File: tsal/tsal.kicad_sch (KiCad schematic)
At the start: 22 parts, among them J1 Conn_01x04, Q1 BUK7M9R5-40H, Q2 BUK7M9R5-40H

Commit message: feat(tsal): updated schematic and pcb
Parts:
- removed D1, D2, D6, D7: 150283RS73103, footprints:Wurth_WL-SMTW, symbol Device:LED
- removed D3, D4, D8, D9: 150283GS73103, footprints:Wurth_WL-SMTW, symbol Device:LED
- removed Q1, Q2: BUK7M9R5-40H, Package_TO_SOT_SMD:LFPAK33, symbol Transistor_FET:BUK7M9R9-60EX
- removed R1, R20, R22, R23, R3, R4: 27, Resistor_SMD:R_2512_6332Metric, symbol Device:R
- added H1, H2, H3: MountingHole, MountingHole:MountingHole_3.2mm_M3, symbol Mechanical:MountingHole
- added J2: Conn_01x03, Connector_Molex:Molex_Micro-Fit_3.0_43650-0315_1x03_P3.00mm_Vertical, symbol Connector_Generic:Conn_01x03
- added Q1, Q2: FDN359BN, Package_TO_SOT_SMD:SOT-23, symbol SUFST:FDN359BN
- J1: footprint Connector_Molex:Molex_Micro-Fit_3.0_43650-0400_1x04_P3.00mm_Horizontal -> Connector_Molex:Molex_Micro-Fit_3.0_43650-0415_1x04_P3.00mm_Vertical
- renumbered R21 to R1
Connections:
- net +12V: now also J2.1 (Pin_1)
- net GND: now also Q1.2 (S), Q2.2 (S)
- net at R2.1: now also J2.2 (Pin_2)
- net at R1.1: now also J2.3 (Pin_3)
- net at R1.2: now also Q1.3 (D)
- net at R2.2: now also Q2.3 (D)
- net GREEN_LED_ON renamed GREEN_LED ON
- net GREEN_LED ON: now also Q2.1 (G)
- net RED_LED_ON renamed RED_LED ON
- net RED_LED ON: now also Q1.1 (G)
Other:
- note removed: "LEDs rated for 180mA. ~3V drop each, so ~6V across resistor. R = 54 gives current of 110mA, and 0.33W in each resistor."
- company: (none) -> SUFST
- title: (none) -> TSAL Driver
- moved on the sheet: R1, R6

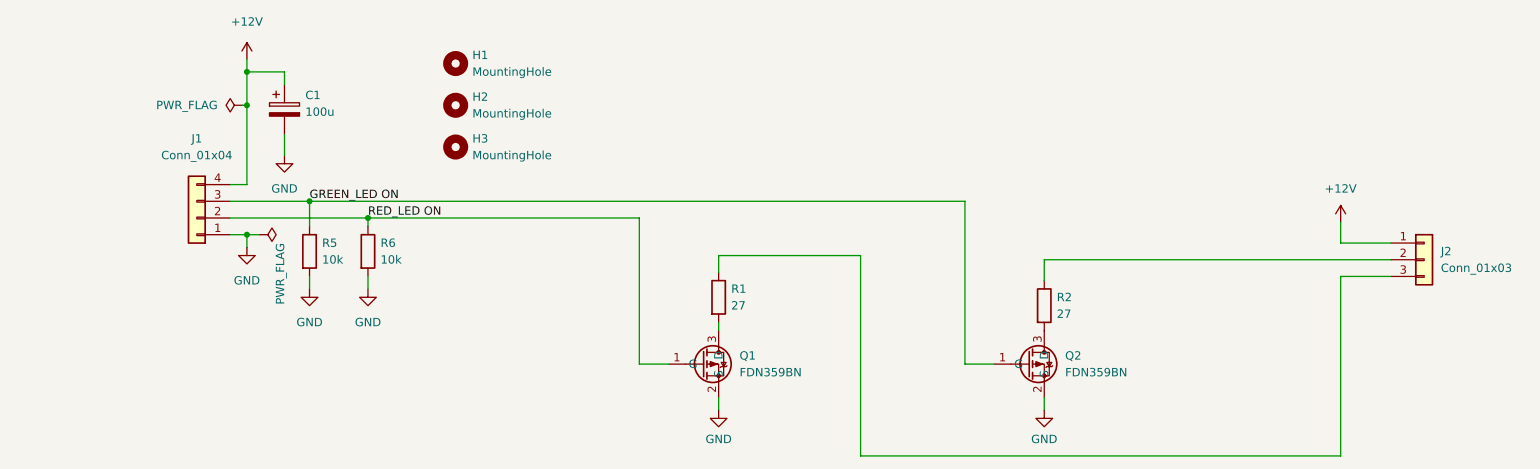
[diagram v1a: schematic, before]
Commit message: feat(tsal) added cad files for the connectors and comments to the schematics
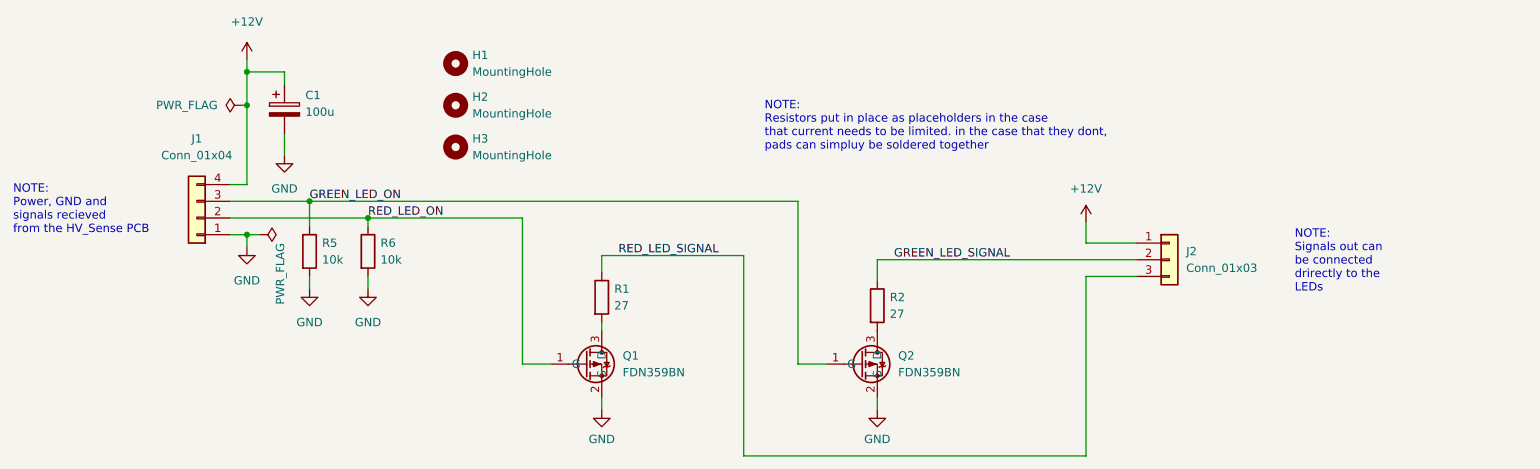
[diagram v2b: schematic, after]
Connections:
- net GREEN_LED_SIGNAL: now reaches J2.2 (Pin_2), R2.1
- net RED_LED_SIGNAL: now reaches J2.3 (Pin_3), R1.1
- net GREEN_LED ON renamed GREEN_LED_ON
- net RED_LED ON renamed RED_LED_ON
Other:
- note added: "NOTE: Power, GND and signals recieved from the HV_Sense PCB"
- note added: "NOTE: Resistors put in place as placeholders in the case that current needs to be limited. in the case that they dont, pads can simpluy be soldered together"
- note added: "NOTE: Signals out can be connected drirectly to the LEDs"
- moved on the sheet: J2, Q1, Q2, R1, R2

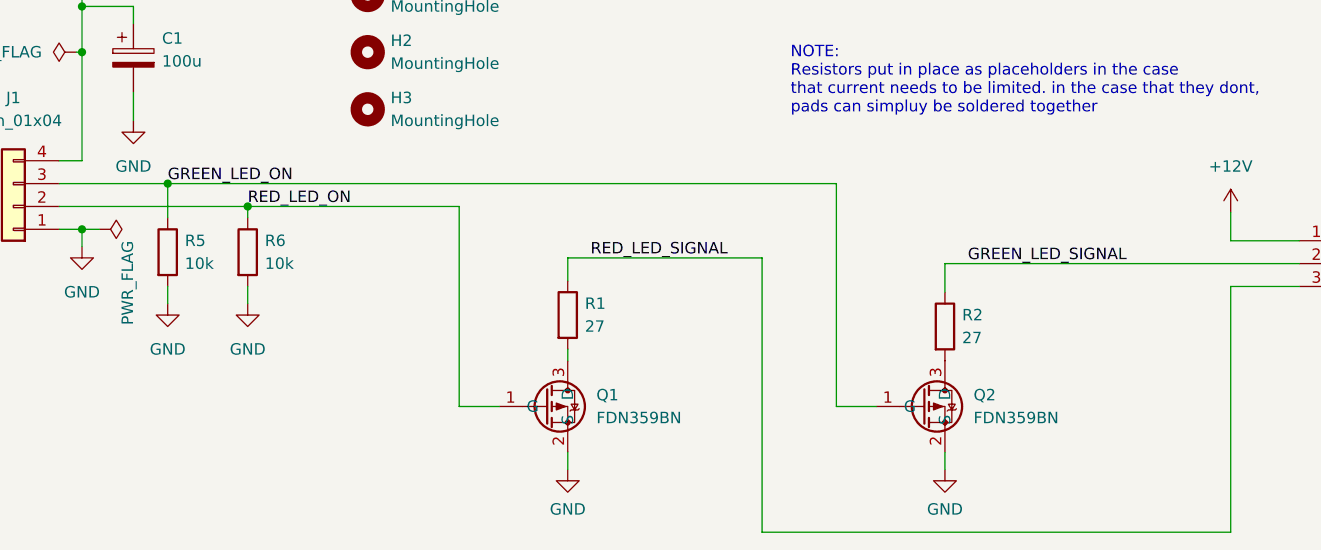
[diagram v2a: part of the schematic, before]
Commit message: feat(tsal) updated tsal driver pcb design: changes in routing, added 12V power plane, added via for Q2, made board smaller, hid mounting hole reference names, moved cad files into common, swapped green_led_on and red_led_on pins for simpler routing, added board name to board, moved symbols library from global to project specific
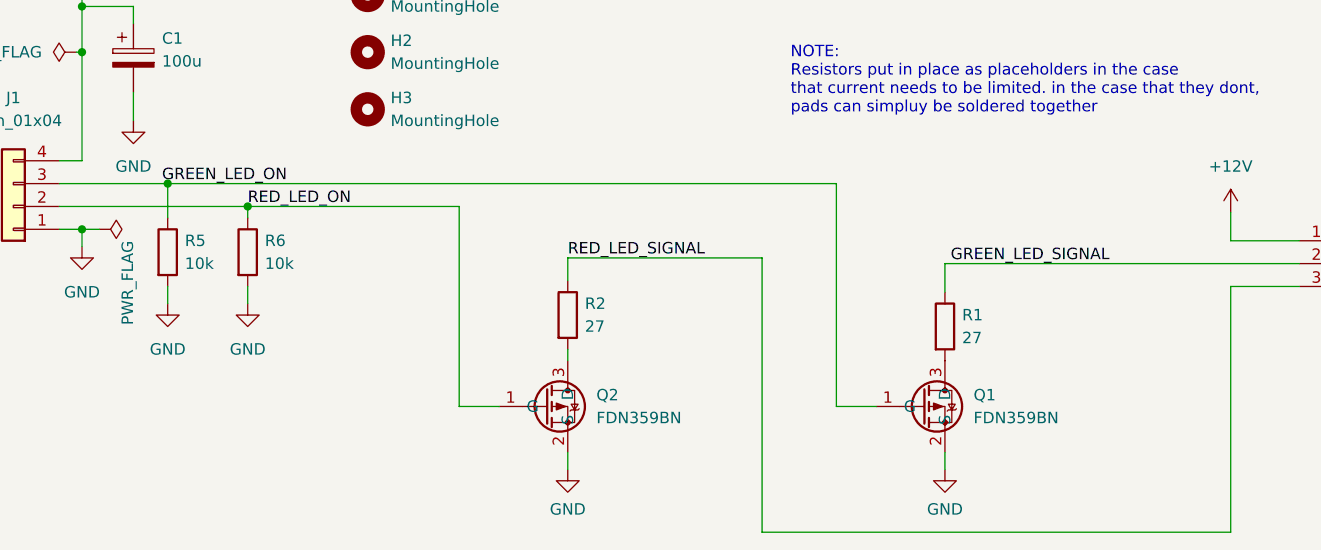
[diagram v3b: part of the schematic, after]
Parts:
- renumbered Q2 to Q1, Q1 to Q2, R2 to R1, R1 to R2
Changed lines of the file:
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@@
     (comment 1 "STAG 9")
     (comment 2 "Marek Frodyma")
+    (comment 3 "Tim Brewis")
   )
   (junction (at 74.295 100.965) (diameter 0) (color 0 0 0 0)
@@
     (effects (font (size 1.27 1.27)) (justify left bottom))
   )
-  (label "GREEN_LED_ON" (at 65.405 98.425 0)
-    (effects (font (size 1.27 1.27)) (justify left bottom))
-  )
-  (label "RED_LED_SIGNAL" (at 112.395 106.68 0)
-    (effects (font (size 1.27 1.27)) (justify left bottom))
-  )
-  (label "GREEN_LED_SIGNAL" (at 154.305 107.315 0)
+  (label "GREEN_LED_ON" (at 64.77 98.425 0)
+    (effects (font (size 1.27 1.27)) (justify left bottom))
+  )
+  (label "RED_LED_SIGNAL" (at 109.855 106.68 0)
+    (effects (font (size 1.27 1.27)) (justify left bottom))
+  )
+  (label "GREEN_LED_SIGNAL" (at 152.4 107.315 0)
     (effects (font (size 1.27 1.27)) (justify left bottom))
   )
@@
   (symbol (lib_id "SUFST:FDN359BN") (at 109.855 123.19 0) (unit 1)
     (in_bom yes) (on_board yes) (fields_autoplaced)
-    (property "Reference" "Q1" (id 0) (at 113.03 121.9199 0)
+    (property "Reference" "Q2" (id 0) (at 113.03 121.9199 0)
       (effects (font (size 1.27 1.27)) (justify left))
     )
@@
   (symbol (lib_id "Device:R") (at 151.765 114.3 0) (unit 1)
     (in_bom yes) (on_board yes) (fields_autoplaced)
-    (property "Reference" "R2" (id 0) (at 153.67 113.0299 0)
+    (property "Reference" "R1" (id 0) (at 153.67 113.0299 0)
       (effects (font (size 1.27 1.27)) (justify left))
     )
@@
   (symbol (lib_id "Device:R") (at 109.855 113.03 0) (unit 1)
     (in_bom yes) (on_board yes) (fields_autoplaced)
-    (property "Reference" "R1" (id 0) (at 111.76 111.7599 0)
+    (property "Reference" "R2" (id 0) (at 111.76 111.7599 0)
       (effects (font (size 1.27 1.27)) (justify left))
     )
@@
   (symbol (lib_id "SUFST:FDN359BN") (at 151.765 123.19 0) (unit 1)
     (in_bom yes) (on_board yes) (fields_autoplaced)
-    (property "Reference" "Q2" (id 0) (at 154.94 121.9199 0)
+    (property "Reference" "Q1" (id 0) (at 154.94 121.9199 0)
       (effects (font (size 1.27 1.27)) (justify left))
     )
@@
       (reference "J2") (unit 1) (value "Conn_01x03") (footprint "Connector_Molex:Molex_Micro-Fit_3.0_43650-0315_1x03_P3.00mm_Vertical")
     )
+    (path "/d637c8c6-252e-44e0-af93-26ba66bbb43d"
+      (reference "Q1") (unit 1) (value "FDN359BN") (footprint "Package_TO_SOT_SMD:SOT-23")
+    )
     (path "/025242f6-9d86-40cc-a4c7-a3dabe68fe74"
-      (reference "Q1") (unit 1) (value "FDN359BN") (footprint "Package_TO_SOT_SMD:SOT-23")
-    )
-    (path "/d637c8c6-252e-44e0-af93-26ba66bbb43d"
       (reference "Q2") (unit 1) (value "FDN359BN") (footprint "Package_TO_SOT_SMD:SOT-23")
     )
+    (path "/1f196da2-5d02-45f7-8267-97c1835b1cf7"
+      (reference "R1") (unit 1) (value "27") (footprint "Resistor_SMD:R_2512_6332Metric")
+    )
     (path "/58e6c009-e544-480b-9137-f8ce2f581d13"
-      (reference "R1") (unit 1) (value "27") (footprint "Resistor_SMD:R_2512_6332Metric")
-    )
-    (path "/1f196da2-5d02-45f7-8267-97c1835b1cf7"
       (reference "R2") (unit 1) (value "27") (footprint "Resistor_SMD:R_2512_6332Metric")
     )

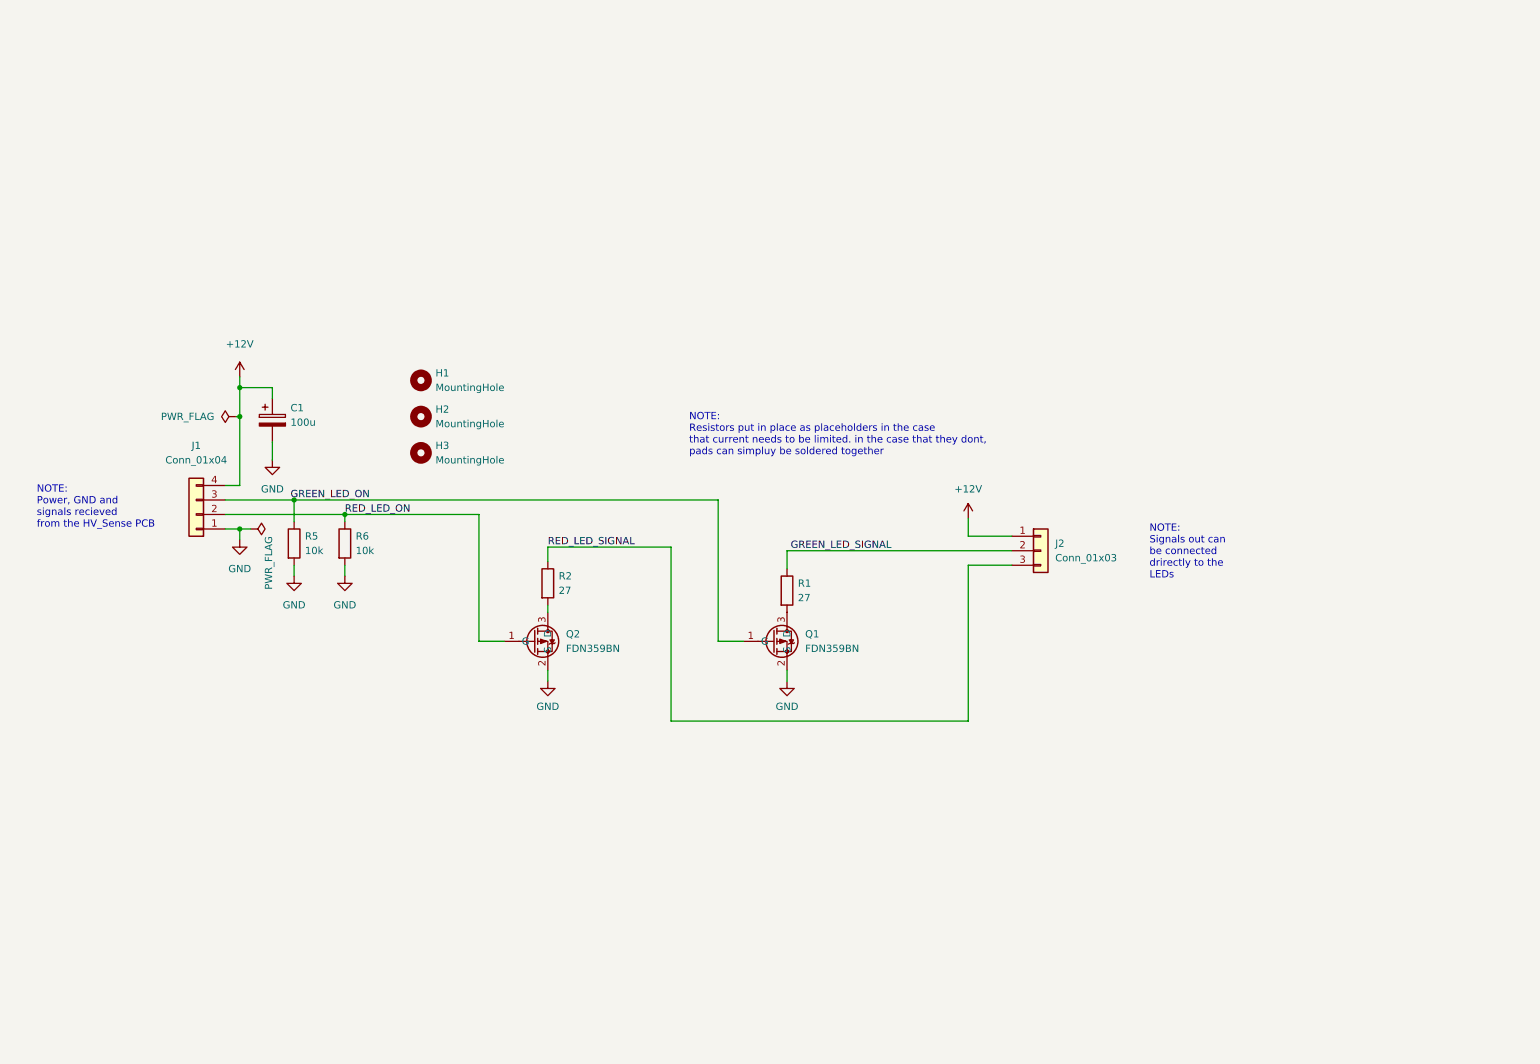
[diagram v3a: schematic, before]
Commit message: feat(tsal): completed psc schematic and layout
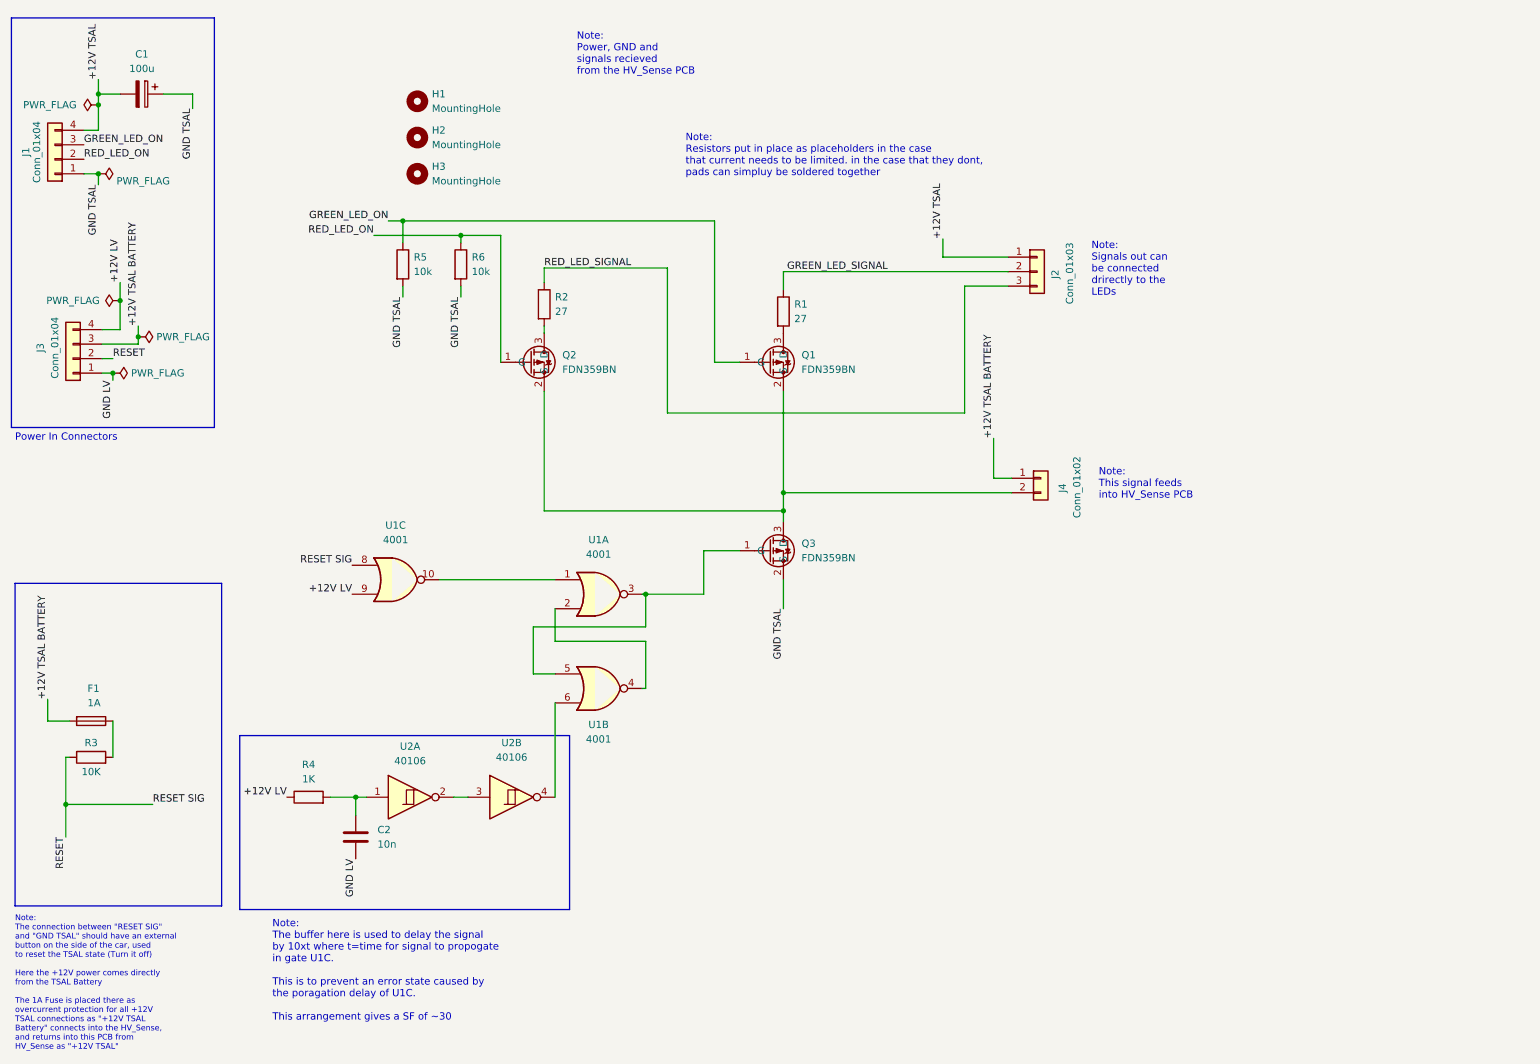
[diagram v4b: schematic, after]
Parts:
- added C2: 10n, Capacitor_SMD:C_0805_2012Metric_Pad1.18x1.45mm_HandSolder, symbol Device:C
- added F1: 1A, Fuse:Fuse_Littelfuse_395Series, symbol Device:Fuse
- added J3: Conn_01x04, Connector_Molex:Molex_Micro-Fit_3.0_43650-0415_1x04_P3.00mm_Vertical, symbol Connector_Generic:Conn_01x04
- added J4: Conn_01x02, Connector_Molex:Molex_Micro-Fit_3.0_43650-0215_1x02_P3.00mm_Vertical, symbol Connector_Generic:Conn_01x02
- added Q3: FDN359BN, Package_TO_SOT_SMD:SOT-23, symbol SUFST:FDN359BN
- added R3: 10K, Resistor_SMD:R_0805_2012Metric_Pad1.20x1.40mm_HandSolder, symbol Device:R
- added R4: 1K, Resistor_SMD:R_0805_2012Metric_Pad1.20x1.40mm_HandSolder, symbol Device:R
- added U1: 4001, Package_SO:SOIC-14_3.9x8.7mm_P1.27mm, symbol 4xxx:4001
- added U2: 40106, Package_SO:SO-14_3.9x8.65mm_P1.27mm, symbol 4xxx:40106
- C1: Order Number (none) -> 710-860020573008; Supplier (none) -> Mouser
- J1, J2: Supplier (none) -> TE
- Q1, Q2: Order Number (none) -> 512-FDN359BN; Supplier (none) -> Mouser
- R1, R2: footprint Resistor_SMD:R_2512_6332Metric -> Resistor_SMD:R_0805_2012Metric_Pad1.20x1.40mm_HandSolder
- R5, R6: footprint Resistor_SMD:R_0603_1608Metric -> Resistor_SMD:R_0805_2012Metric_Pad1.20x1.40mm_HandSolder
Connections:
- net +12V renamed +12V TSAL
- net +12V TSAL: now also C1.2; no longer C1.1
- net GND renamed GND TSAL
- net GND TSAL: now also C1.1, Q3.2 (S); no longer C1.2, Q1.2 (S), Q2.2 (S)
- new net: J4.2 (Pin_2), Q1.2 (S), Q2.2 (S), Q3.3 (D)
- new net: U1.2, U1.4
- new net: Q3.1 (G), U1.3, U1.5
- new net: U1.6, U2.4
- new net: C2.1, R4.2, U2.1
- new net: F1.1, R3.2
- new net: U1.1, U1.10
- new net: U2.2, U2.3
- new net +12V LV: J3.4 (Pin_4), R4.1, U1.9
- new net +12V TSAL BATTERY: F1.2, J3.3 (Pin_3), J4.1 (Pin_1)
- new net GND LV: C2.2, J3.1 (Pin_1)
- new net RESET: J3.2 (Pin_2), R3.1, U1.8
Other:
- note added: "Note: Power, GND and signals recieved from the HV_Sense PCB"
- note added: "Note: Resistors put in place as placeholders in the case that current needs to be limited. in the case that they dont, pads can simpluy be soldered together"
- note added: "Note: Signals out can be connected drirectly to the LEDs"
- note added: "Note: The buffer here is used to delay the signal by 10xt where t=time for signal to propogate in gate U1C. This is to prevent an error state caused by the poragation delay of U1C. This arrangement gives a SF of ~30"
- note added: "Note: The connection between "RESET SIG" and "GND TSAL" should have an external button on the side of the car, used to reset the TSAL state (Turn it off) Here the +12V power comes directly from the TSAL Battery The 1A Fuse is placed there as overcurrent protection for all +12V TSAL connections as "+12V TSAL Battery" connects into the HV_Sense, and returns into this PCB from HV_Sense as "+12V TSAL""
- note added: "Note: This signal feeds into HV_Sense PCB"
- note added: "Power In Connectors"
- note removed: "NOTE: Power, GND and signals recieved from the HV_Sense PCB"
- note removed: "NOTE: Resistors put in place as placeholders in the case that current needs to be limited. in the case that they dont, pads can simpluy be soldered together"
- note removed: "NOTE: Signals out can be connected drirectly to the LEDs"
- title: TSAL Driver -> TSAL Control
- moved on the sheet: C1, H1, H2, H3, J2, Q1, Q2, R1, R2, R5, R6
